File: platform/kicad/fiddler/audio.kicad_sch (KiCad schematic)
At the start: 54 parts, among them J4 Screw_Terminal_01x02, SW3 SW_Push, U2 TAS5731MPHP

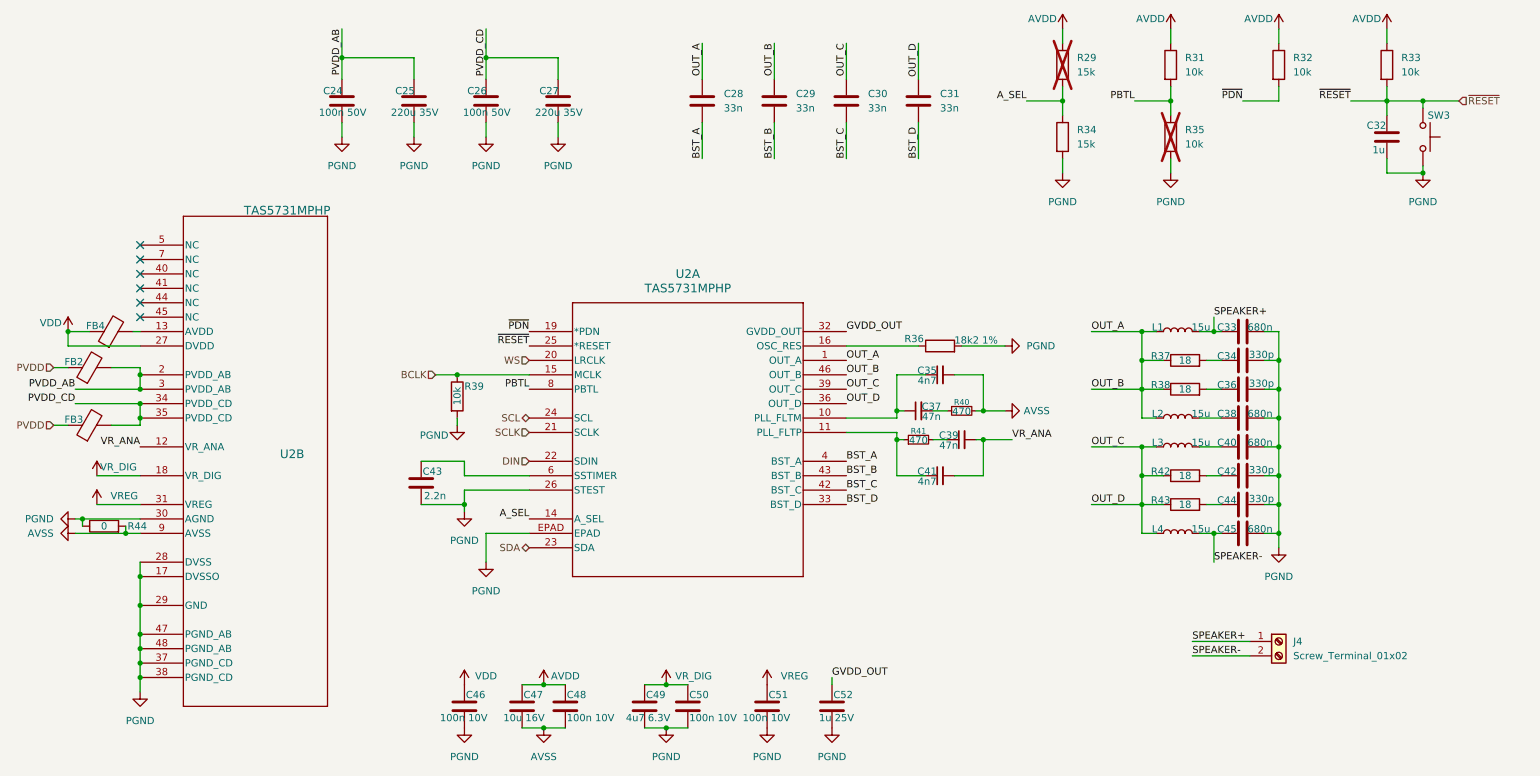
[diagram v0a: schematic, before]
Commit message: Fiddler Ray Speaker: Complete first revision
This change completes the first iteration schematic and layout for the fiddler ray speaker PCB.
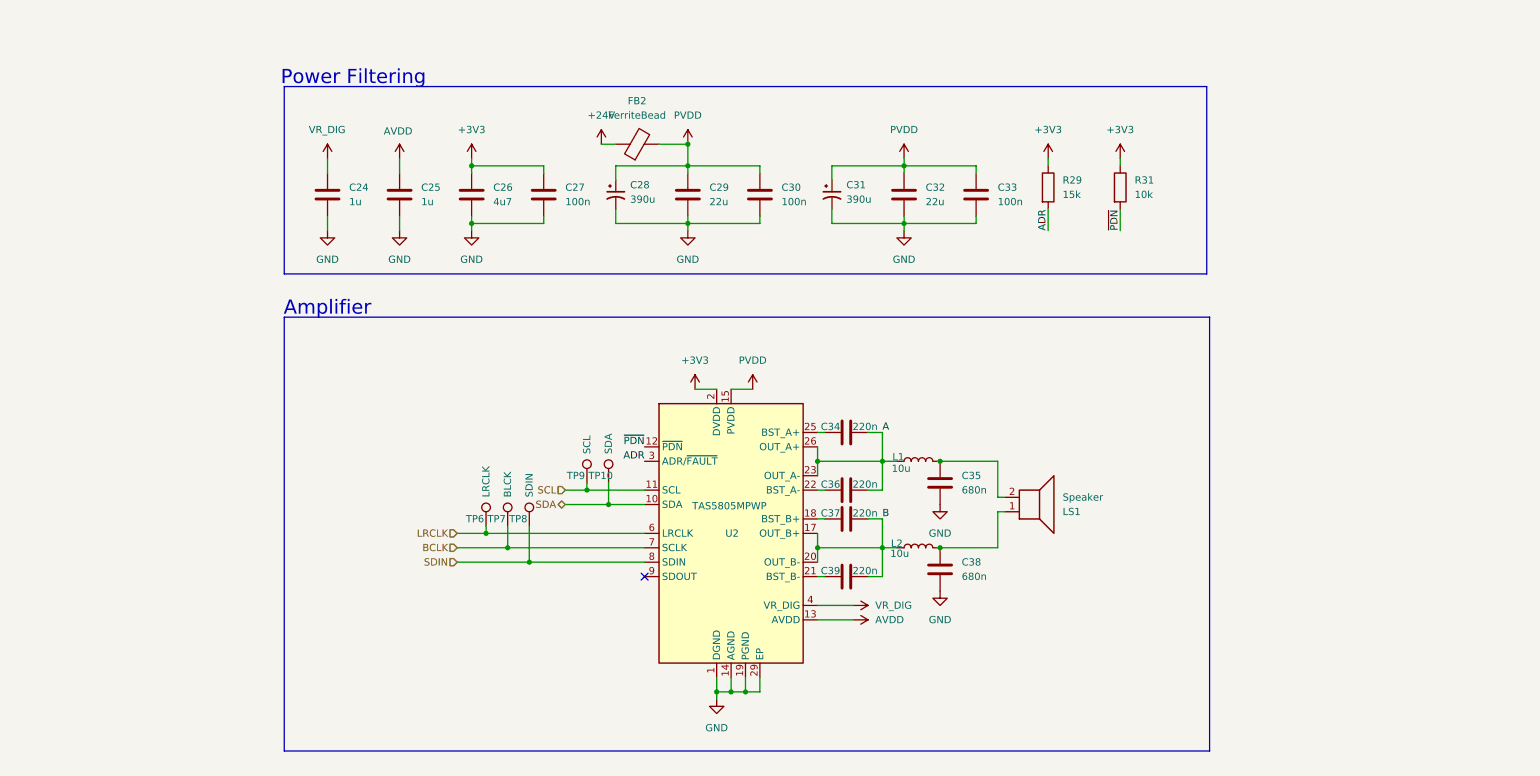
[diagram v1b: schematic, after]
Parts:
- removed C28, C31: 33n, Capacitor_SMD:C_0805_2012Metric, symbol Device:C
- removed C35, C41: 4n7, Capacitor_SMD:C_0201_0603Metric, symbol Device:C_Small
- removed C37, C39: 47n, Capacitor_SMD:C_0201_0603Metric, symbol Device:C_Small
- removed C40, C45: 680n, Capacitor_SMD:C_0201_0603Metric, symbol Device:C
- removed C42, C44: 330p, Capacitor_SMD:C_0201_0603Metric, symbol Device:C
- removed C43: 2.2n, Capacitor_SMD:C_0201_0603Metric, symbol Device:C
- removed C46, C48, C50, C51: 100n 10V, Capacitor_SMD:C_0603_1608Metric, symbol Device:C
- removed C47: 10u 16V, Capacitor_SMD:C_0603_1608Metric, symbol Device:C
- removed C49: 4u7 6.3V, Capacitor_SMD:C_0603_1608Metric, symbol Device:C
- removed C52: 1u 25V, Capacitor_SMD:C_0603_1608Metric, symbol Device:C
- removed FB3, FB4: 120/4A, Resistor_SMD:R_0603_1608Metric, symbol Device:FerriteBead
- removed J4: Screw_Terminal_01x02, TerminalBlock:TerminalBlock_Wuerth_691311400102_P7.62mm, symbol Connector:Screw_Terminal_01x02
- removed L3, L4: 15u, Inductor_SMD:L_Changjiang_FNR8040S, symbol Device:L
- removed R32, R33, R35, R39: 10k, Resistor_SMD:R_0603_1608Metric, symbol Device:R
- removed R34: 15k, Resistor_SMD:R_0603_1608Metric, symbol Device:R
- removed R36: 18k2 1%, Resistor_SMD:R_0603_1608Metric, symbol Device:R
- removed R37, R38, R42, R43: 18, Resistor_SMD:R_0603_1608Metric, symbol Device:R
- removed R40, R41: 470, Resistor_SMD:R_0603_1608Metric, symbol Device:R_Small
- removed R44: 0, Resistor_SMD:R_0603_1608Metric, symbol Device:R
- removed SW3: SW_Push, Resistor_SMD:R_0603_1608Metric, symbol Switch:SW_Push
- removed U2: TAS5731MPHP, AusOcean:PHP48_5P17X4P04_TEX, symbol AusOcean:TAS5731MPHP
- added C28, C31: 390u, Capacitor_SMD:CP_Elec_10x10, symbol Device:C_Polarized_Small_US
- added C35: 680n, Capacitor_SMD:C_0805_2012Metric, symbol Device:C
- added C37, C39: 220n, Capacitor_SMD:C_0603_1608Metric, symbol Device:C
- added LS1: Speaker, TerminalBlock_Phoenix:TerminalBlock_Phoenix_MPT-0,5-2-2.54_1x02_P2.54mm_Horizontal, symbol Device:Speaker
- added TP10: SDA, TestPoint:TestPoint_Pad_D1.0mm, symbol Connector:TestPoint
- added TP6: LRCLK, TestPoint:TestPoint_Pad_D1.0mm, symbol Connector:TestPoint
- added TP7: BLCK, TestPoint:TestPoint_Pad_D1.0mm, symbol Connector:TestPoint
- added TP8: SDIN, TestPoint:TestPoint_Pad_D1.0mm, symbol Connector:TestPoint
- added TP9: SCL, TestPoint:TestPoint_Pad_D1.0mm, symbol Connector:TestPoint
- added U2: TAS5805MPWP, Package_SO:TSSOP-28-1EP_4.4x9.7mm_P0.65mm_EP3.4x9.7mm_Mask3.1x4.05mm_ThermalVias, symbol Amplifier_Audio:TAS5805MPWP
- C24: value 100n 50V -> 1u; footprint Capacitor_SMD:C_0805_2012Metric -> Capacitor_SMD:C_0603_1608Metric
- C25: value 220u 35V -> 1u; footprint Capacitor_SMD:C_0805_2012Metric -> Capacitor_SMD:C_0603_1608Metric
- C26: value 100n 50V -> 4u7; footprint Capacitor_SMD:C_0805_2012Metric -> Capacitor_SMD:C_0603_1608Metric
- C27: value 220u 35V -> 100n; footprint Capacitor_SMD:C_0805_2012Metric -> Capacitor_SMD:C_0603_1608Metric
- C29: value 33n -> 22u; footprint Capacitor_SMD:C_0805_2012Metric -> Capacitor_SMD:C_0603_1608Metric
- C30: value 33n -> 100n; footprint Capacitor_SMD:C_0805_2012Metric -> Capacitor_SMD:C_0402_1005Metric
- C32: value 1u -> 22u; footprint Capacitor_SMD:C_0201_0603Metric -> Capacitor_SMD:C_0603_1608Metric
- C33: value 680n -> 100n; footprint Capacitor_SMD:C_0201_0603Metric -> Capacitor_SMD:C_0402_1005Metric
- C34, C36: value 330p -> 220n; footprint Capacitor_SMD:C_0201_0603Metric -> Capacitor_SMD:C_0603_1608Metric
- C38: footprint Capacitor_SMD:C_0201_0603Metric -> Capacitor_SMD:C_0805_2012Metric
- FB2: value 120/4A -> FerriteBead
- L1, L2: value 15u -> 10u; footprint Inductor_SMD:L_Changjiang_FNR8040S -> Inductor_SMD:L_Changjiang_FXL1050
- R29: now fitted
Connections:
- net BST_C is gone; now on net GND: C30.2
- net OUT_C is gone; now on net PVDD: C30.1
- net PBTL is gone; now on net ~{PDN}: R31.2
- net ~{RESET} is gone; now on net PVDD: C32.1
- net AVDD: now also C25.1, U2.13 (AVDD); no longer R29.1, R31.1
- net BCLK: now also TP7.1, U2.7 (SCLK)
- net PVDD: now also C29.1, C33.1, FB2.2, C28.1, C31.1, U2.15 (PVDD), U2.16 (PVDD), U2.27 (PVDD), U2.28 (PVDD); no longer FB2.1
- net SCL: now also TP9.1, U2.11 (SCL)
- net SDA: now also TP10.1, U2.10 (SDA)
- net VR_DIG: now also C24.1, U2.4 (VR_DIG)
- net ~{PDN}: now also U2.12 (~{PDN})
- net at C38.1, L2.2: now also LS1.1
- net at C34.1: now also U2.25 (BST_A+)
- net at C36.1: now also U2.22 (BST_A-)
- net A_SEL renamed ADR
- net ADR: now also U2.3 (ADR/~{FAULT})
- net BST_B renamed GND
- net GND: now also C24.2, C25.2, C26.2, C27.2, C32.2, C33.2, C38.2, C28.2, C31.2, C35.2, U2.1 (DGND), U2.14 (AGND), U2.19 (PGND), U2.24 (PGND), U2.29 (EP), U2.5 (DGND)
- removed net OUT_A: C29.1, L1.1, L2.1
- removed net PGND: C24.2, C25.2, C26.2, C27.2, C32.2, C33.2, C34.2, C36.2, C38.2
- removed net PVDD_AB: C24.1, C25.1, FB2.2
- net PVDD_CD renamed +3V3
- net +3V3: now also R29.1, R31.1, U2.2 (DVDD)
- net SPEAKER+: no longer names the net of L1.2
- net SPEAKER+: now also C35.1, LS1.2; no longer C33.1
- new net: C37.1, U2.18 (BST_B+)
- new net: C39.1, U2.21 (BST_B-)
- new net +24V: FB2.1
- new net A: C34.2, C36.2, L1.1, U2.23 (OUT_A-), U2.26 (OUT_A+)
- new net B: C37.2, C39.2, L2.1, U2.17 (OUT_B+), U2.20 (OUT_B-)
- new net LRCLK: TP6.1, U2.6 (LRCLK)
- new net SDIN: TP8.1, U2.8 (SDIN)
- no-connect marks 6 -> 1
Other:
- note added: "Amplifier"
- note added: "Power Filtering"
- company: (none) -> The Australian Ocean Laboratory
- title: (none) -> Fiddler Ray Speaker Unit V1

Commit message: Fiddler Ray Speaker: Production rev A
This change adds additional data to components to populate SPN for
the BOM via JLC
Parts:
- C24, C25: LCSC Part # (none) -> C15849
- C26: LCSC Part # (none) -> C19666
- C27: LCSC Part # (none) -> C14663
- C28, C31: LCSC Part # (none) -> C359223; Voltage Rating (none) -> 50V
- C29, C32: footprint Capacitor_SMD:C_0603_1608Metric -> Capacitor_SMD:C_2220_5750Metric; LCSC Part # (none) -> C784103; Voltage Rating (none) -> 50V
- C30, C33: LCSC Part # (none) -> C77020; Voltage Rating (none) -> 50V
- C34, C36, C37, C39: LCSC Part # (none) -> C64705; Voltage Rating (none) -> 50V
- C35, C38: LCSC Part # (none) -> C107133; Voltage Rating (none) -> 50V
- FB2: footprint Resistor_SMD:R_0603_1608Metric -> Inductor_SMD:L_0603_1608Metric; LCSC Part # (none) -> C14709
- L1, L2: LCSC Part # (none) -> C5359264
- LS1: LCSC Part # (none) -> C3029316
- TP10, TP6, TP7, TP8, TP9: now left out of the parts list
- U2: LCSC Part # (none) -> C478472
